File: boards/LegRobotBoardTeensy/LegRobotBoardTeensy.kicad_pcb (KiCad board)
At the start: 2 copper layers, 87.5 x 55 mm, 50 parts, among them J1 B5B-XH-A, J10 B4B-XH-A, J11 B3B-XH-A, J2 B4B-XH-A, J3 B3B-XH-A, J4 B3B-XH-A, J5 B4B-XH-A, J6 B2B-XH-A, J7 B2B-XH-A, J8 B4B-XH-A, J9 B4B-XH-A, Q1 SMMBT3904LT1G, U1 Teensy4.0, U2 TLC555CDR, U3 SN74HC08DR, U4 SN74HC08DR

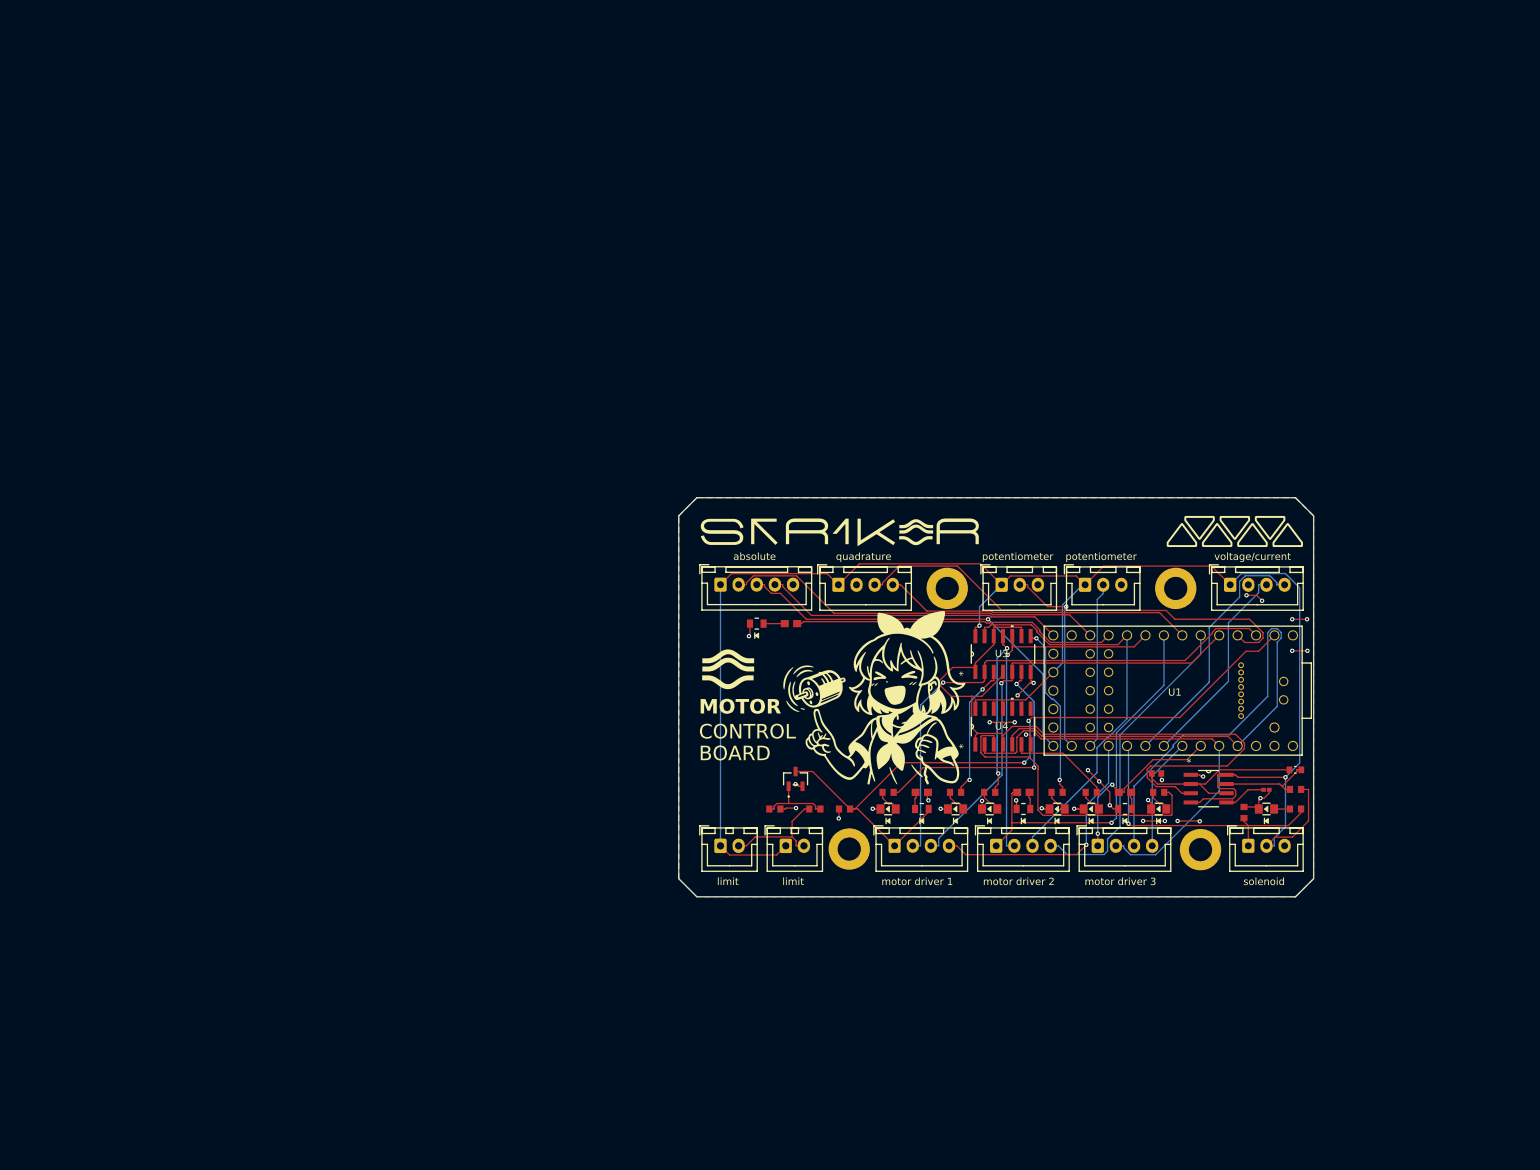
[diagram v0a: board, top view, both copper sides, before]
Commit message: Finalize and order leg board
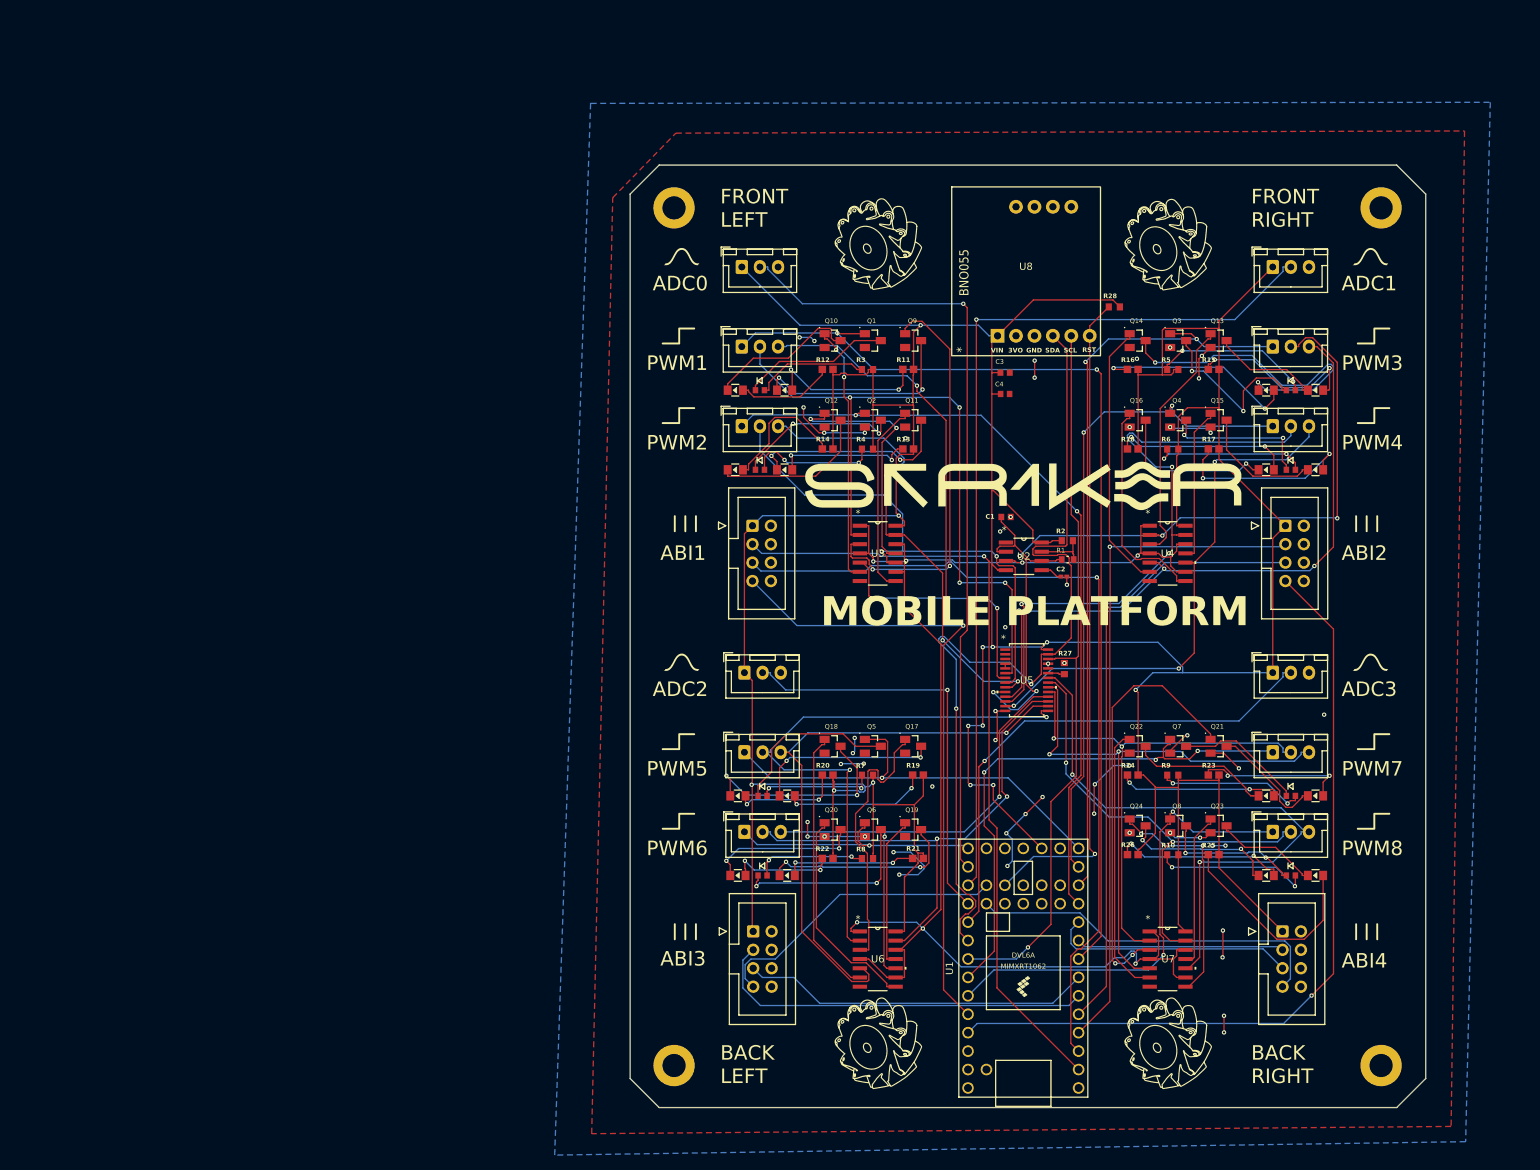
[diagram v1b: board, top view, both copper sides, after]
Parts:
- added C3: 1uF, CC0603JRX7R7BB105:CC0603JRX7R7BB105, F.Cu at (145.0, 56.8)
- added C4: 100nF, CC0603KRX7R9BB104:CC0603KRX7R9BB104, F.Cu at (145.0, 59.7)
- added D12: BLUELED, 150080BS75000:150080BS75000_Modified, F.Cu at (107.8, 70.2)
- added D13: BLUELED, 150080BS75000:150080BS75000_Modified, F.Cu at (187.8, 59.2)
- added D14: BLUELED, 150080BS75000:150080BS75000_Modified, F.Cu at (181.0, 59.2)
- added D15: BLUELED, 150080BS75000:150080BS75000_Modified, F.Cu at (187.8, 70.2)
- added D16: BLUELED, 150080BS75000:150080BS75000_Modified, F.Cu at (181.0, 70.2)
- added D17: BLUELED, 150080BS75000:150080BS75000_Modified, F.Cu at (114.9, 115.1)
- added D18: BLUELED, 150080BS75000:150080BS75000_Modified, F.Cu at (108.2, 115.1)
- added D19: BLUELED, 150080BS75000:150080BS75000_Modified, F.Cu at (114.9, 126.1)
- added D20: BLUELED, 150080BS75000:150080BS75000_Modified, F.Cu at (108.2, 126.1)
- added D21: BLUELED, 150080BS75000:150080BS75000_Modified, F.Cu at (187.8, 115.1)
- added D22: BLUELED, 150080BS75000:150080BS75000_Modified, F.Cu at (181.0, 115.1)
- added D23: BLUELED, 150080BS75000:150080BS75000_Modified, F.Cu at (187.8, 126.1)
- added D24: BLUELED, 150080BS75000:150080BS75000_Modified, F.Cu at (181.0, 126.1)
- added J12: B3B-XH-A, Connector_JST:JST_XH_B3B-XH-A_1x03_P2.50mm_Vertical, F.Cu at (181.9, 109.1)
- added J13: B3B-XH-A, Connector_JST:JST_XH_B3B-XH-A_1x03_P2.50mm_Vertical, F.Cu at (181.9, 120.0)
- added J14: IDC, Connector_IDC:IDC-Header_2x04_P2.54mm_Vertical, F.Cu at (183.6, 77.9)
- added J15: IDC, Connector_IDC:IDC-Header_2x04_P2.54mm_Vertical, F.Cu at (110.3, 133.8)
- added J16: IDC, Connector_IDC:IDC-Header_2x04_P2.54mm_Vertical, F.Cu at (183.2, 133.8)
- added Q10: MMBT3904LT1G, SMMBT3904LT1G:MMBT3904LT1G, F.Cu at (121.2, 52.3)
- added Q11: MMBT3904LT1G, SMMBT3904LT1G:MMBT3904LT1G, F.Cu at (132.3, 63.3)
- added Q12: MMBT3904LT1G, SMMBT3904LT1G:MMBT3904LT1G, F.Cu at (121.2, 63.3)
- added Q13: MMBT3904LT1G, SMMBT3904LT1G:MMBT3904LT1G, F.Cu at (174.4, 52.3)
- added Q14: MMBT3904LT1G, SMMBT3904LT1G:MMBT3904LT1G, F.Cu at (163.2, 52.3)
- added Q15: MMBT3904LT1G, SMMBT3904LT1G:MMBT3904LT1G, F.Cu at (174.4, 63.3)
- added Q16: MMBT3904LT1G, SMMBT3904LT1G:MMBT3904LT1G, F.Cu at (163.2, 63.3)
- added Q17: MMBT3904LT1G, SMMBT3904LT1G:MMBT3904LT1G, F.Cu at (132.3, 108.3)
- added Q18: MMBT3904LT1G, SMMBT3904LT1G:MMBT3904LT1G, F.Cu at (121.2, 108.3)
- added Q19: MMBT3904LT1G, SMMBT3904LT1G:MMBT3904LT1G, F.Cu at (132.3, 119.7)
- added Q2: MMBT3904LT1G, SMMBT3904LT1G:MMBT3904LT1G, F.Cu at (126.8, 63.3)
- added Q20: MMBT3904LT1G, SMMBT3904LT1G:MMBT3904LT1G, F.Cu at (121.2, 119.7)
- added Q21: MMBT3904LT1G, SMMBT3904LT1G:MMBT3904LT1G, F.Cu at (174.4, 108.3)
- added Q22: MMBT3904LT1G, SMMBT3904LT1G:MMBT3904LT1G, F.Cu at (163.2, 108.3)
- added Q23: MMBT3904LT1G, SMMBT3904LT1G:MMBT3904LT1G, F.Cu at (174.4, 119.2)
- added Q24: MMBT3904LT1G, SMMBT3904LT1G:MMBT3904LT1G, F.Cu at (163.2, 119.2)
- added Q3: MMBT3904LT1G, SMMBT3904LT1G:MMBT3904LT1G, F.Cu at (168.8, 52.3)
- added Q4: MMBT3904LT1G, SMMBT3904LT1G:MMBT3904LT1G, F.Cu at (168.8, 63.3)
- added Q5: MMBT3904LT1G, SMMBT3904LT1G:MMBT3904LT1G, F.Cu at (126.8, 108.3)
- added Q6: MMBT3904LT1G, SMMBT3904LT1G:MMBT3904LT1G, F.Cu at (126.8, 119.7)
- added Q7: MMBT3904LT1G, SMMBT3904LT1G:MMBT3904LT1G, F.Cu at (168.8, 108.3)
- added Q8: MMBT3904LT1G, SMMBT3904LT1G:MMBT3904LT1G, F.Cu at (168.8, 119.2)
- added Q9: MMBT3904LT1G, SMMBT3904LT1G:MMBT3904LT1G, F.Cu at (132.3, 52.3)
- added R18: 150R, RC0603FR-07150RL:RESC1607X60N, F.Cu at (162.6, 67.3)
- added R19: 150R, RC0603FR-07150RL:RESC1607X60N, F.Cu at (133.0, 112.2)
- added R20: 150R, RC0603FR-07150RL:RESC1607X60N, F.Cu at (120.5, 112.2)
- added R21: 150R, RC0603FR-07150RL:RESC1607X60N, F.Cu at (133.0, 123.7)
- added R22: 150R, RC0603FR-07150RL:RESC1607X60N, F.Cu at (120.5, 123.7)
- added R23: 150R, RC0603FR-07150RL:RESC1607X60N, F.Cu at (173.7, 112.2)
- added R24: 150R, RC0603FR-07150RL:RESC1607X60N, F.Cu at (162.6, 112.2)
- added R25: 150R, RC0603FR-07150RL:RESC1607X60N, F.Cu at (173.7, 123.2)
- added R26: 150R, RC0603FR-07150RL:RESC1607X60N, F.Cu at (162.6, 123.2)
- added R27: 10K, CRCW060310K0FKEA:CRCW060310K0FKEA, F.Cu at (153.2, 97.5)
- added R28: 10K, CRCW060310K0FKEA:CRCW060310K0FKEA, F.Cu at (160.0, 47.7)
- added U5: PCA9685PW_118, PCA9685PW,118:PCA9685PW,118, F.Cu at (148.0, 99.2)
- added U6: SN74HC08DR, SN74HC08DR:SN74HC08DR, F.Cu at (127.4, 137.6)
- added U7: SN74HC08DR, SN74HC08DR:SN74HC08DR, F.Cu at (167.4, 137.6)
- added U8: BNO055, BNO055:BNO055, F.Cu at (147.9, 42.6)
- D1, D2, D3, D4, D6, D7: value BLUE LED -> REDLED; footprint 150080BS75000:150080BS75000_Modified -> NCD0603R1:NCD0603R1
- D10, D11: value PINK LED -> BLUELED; footprint XL-2012UPC:LED_XL-2012SURC_XLG -> 150080BS75000:150080BS75000_Modified
- D5, D8: value PINK LED -> REDLED; footprint XL-2012UPC:LED_XL-2012SURC_XLG -> NCD0603R1:NCD0603R1
- D9: value BLUE LED -> BLUELED
- J1: value B5B-XH-A -> IDC; footprint Connector_JST:JST_XH_B5B-XH-A_1x05_P2.50mm_Vertical -> Connector_IDC:IDC-Header_2x04_P2.54mm_Vertical
- J10, J2, J5, J8, J9: value B4B-XH-A -> B3B-XH-A; footprint Connector_JST:JST_XH_B4B-XH-A_1x04_P2.50mm_Vertical -> Connector_JST:JST_XH_B3B-XH-A_1x03_P2.50mm_Vertical
- J6, J7: value B2B-XH-A -> B3B-XH-A; footprint Connector_JST:JST_XH_B2B-XH-A_1x02_P2.50mm_Vertical -> Connector_JST:JST_XH_B3B-XH-A_1x03_P2.50mm_Vertical
- Q1: value SMMBT3904LT1G -> MMBT3904LT1G; footprint SMMBT3904LT1G:SMMBT3904LT1G -> SMMBT3904LT1G:MMBT3904LT1G
- R1: value 150R -> 360K; footprint RCG06031K00FKEA:RCG06031K00FKEA -> RC0603FR-07360KL:RC0603FR-07360KL
- R10, R5: value 470R -> 1K; footprint RC0603FR-07470RL:RC0603FR-07470RL -> RCG06031K00FKEA:RCG06031K00FKEA
- R11: footprint RCG06031K00FKEA:RCG06031K00FKEA -> RC0603FR-07150RL:RESC1607X60N
- R12, R13: value 470R -> 150R; footprint RC0603FR-07470RL:RC0603FR-07470RL -> RC0603FR-07150RL:RESC1607X60N
- R14, R17: value 100K -> 150R; footprint CRCW0603100KFKEA:CRCW0603100KFKEA -> RC0603FR-07150RL:RESC1607X60N
- R15: value 10K -> 150R; footprint CRCW060310K0FKEA:CRCW060310K0FKEA -> RC0603FR-07150RL:RESC1607X60N
- R16: value 360K -> 150R; footprint RC0603FR-07360KL:RC0603FR-07360KL -> RC0603FR-07150RL:RESC1607X60N
- R2: value 150R -> 10K; footprint RCG06031K00FKEA:RCG06031K00FKEA -> CRCW060310K0FKEA:CRCW060310K0FKEA
- R3, R4, R6, R7: value 150R -> 1K
- R8: value 10K -> 1K; footprint CRCW060310K0FKEA:CRCW060310K0FKEA -> RCG06031K00FKEA:RCG06031K00FKEA
- R9: value 100K -> 1K; footprint CRCW0603100KFKEA:CRCW0603100KFKEA -> RCG06031K00FKEA:RCG06031K00FKEA
- U1: footprint Teensy:Teensy40_SMT -> Teensy40:Teensy40
- moved D9 88.0 mm to (114.6, 59.2)
- moved J8 86.3 mm to (181.9, 53.2)
- moved D8 81.4 mm to (184.4, 126.1), turned to 180 degrees
- moved R11 80.8 mm to (131.6, 56.3)
- moved D10 70.1 mm to (107.8, 59.2)
- moved J11 69.5 mm to (109.0, 120.0)
- moved J9 69.3 mm to (181.9, 64.1)
- moved J6 68.9 mm to (108.7, 53.2)
- moved R5 67.8 mm to (168.1, 56.3)
- moved D11 66.2 mm to (114.6, 70.2)
- moved D3 66.1 mm to (184.4, 59.2), turned to 180 degrees
- moved MH1 64.6 mm to (99.3, 34.0)
- moved R12 64.2 mm to (120.5, 56.3), turned to 0 degrees
- moved R3 63.9 mm to (126.0, 56.3)
- moved D1 63.7 mm to (111.2, 59.2), turned to 180 degrees
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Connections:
- D1 pad 1: GND -> Net-(D1-K)
- D1 pad 2: Net-(D1-Pad2) -> Net-(D1-A)
- D10 pad 1: GND -> Net-(D10-K)
- D11 pad 1: GND -> Net-(D11-K)
- D2 pad 1: GND -> Net-(D2-K)
- D2 pad 2: Net-(D2-Pad2) -> Net-(D2-A)
- D3 pad 1: GND -> Net-(D3-K)
- D3 pad 2: Net-(D3-Pad2) -> Net-(D3-A)
- D4 pad 1: GND -> Net-(D4-K)
- D4 pad 2: Net-(D4-Pad2) -> Net-(D4-A)
- D5 pad 1: Net-(D5-Pad1) -> Net-(D5-K)
- D5 pad 2: PWM1EN -> Net-(D5-A)
- D6 pad 1: GND -> Net-(D6-K)
- D6 pad 2: Net-(D6-Pad2) -> Net-(D6-A)
- D7 pad 1: GND -> Net-(D7-K)
- D7 pad 2: Net-(D7-Pad2) -> Net-(D7-A)
- D8 pad 1: GND -> Net-(D8-K)
- D9 pad 1: GND -> Net-(D9-K)
- J1 pad 2: CS -> GND
- J1 pad 3: SCK -> ENCODER1_A
- J1 pad 4: MISO -> GND
- J1 pad 5: GND -> ENCODER1_B
- J10 pad 1: PWM3EN -> PWMEN5
- J10 pad 2: RPWM3 -> RPWM5
- J10 pad 3: LPWM3 -> LPWM5
- J11 pad 1: SIG -> PWMEN6
- J11 pad 2: +3.3V -> RPWM6
- J11 pad 3: GND -> LPWM6
- J2 pad 2: GND -> A0
- J2 pad 3: A -> GND
- J3 pad 2: A0 -> A1
- J4 pad 2: A1 -> A2
- J5 pad 2: GND -> A3
- J5 pad 3: SCL -> GND
- J6 pad 1: +3.3V -> PWMEN1
- J6 pad 2: /PWM1EN_LIMIT_KILL -> RPWM1
- J7 pad 1: +3.3V -> PWMEN2
- J7 pad 2: /PWM1EN_LIMIT_KILL -> RPWM2
- J8 pad 1: PWM1EN -> PWMEN3
- J8 pad 2: RPWM1 -> RPWM3
- J8 pad 3: LPWM1 -> LPWM3
- J9 pad 1: PWM2EN -> PWMEN4
- J9 pad 2: RPWM2 -> RPWM4
- J9 pad 3: LPWM2 -> LPWM4
- Q1 pad 1: Net-(Q1-BASE) -> PWMEN1
- Q1 pad 3: PWM1EN -> Net-(D1-K)
- R1 pad 1: Net-(D1-Pad2) -> /NODE_A
- R1 pad 2: RPWM1A -> /NODE_B
- R10 pad 2: SPIS -> +3.3V
- R11 pad 2: SIG -> +3.3V
- R12 pad 2: PWM2EN -> +3.3V
- R13 pad 2: PWM3EN -> +3.3V
- R14 pad 1: GND -> Net-(D12-A)
- R14 pad 2: Net-(Q1-BASE) -> +3.3V
- R15 pad 1: /NODE_B -> Net-(D13-A)
- R16 pad 1: /NODE_A -> Net-(D14-A)
- R16 pad 2: /NODE_B -> +3.3V
- R17 pad 1: GND -> Net-(D15-A)
- R17 pad 2: SIG -> +3.3V
- R2 pad 1: Net-(D2-Pad2) -> +3.3V
- R2 pad 2: LPWM1A -> /NODE_B
- R3 pad 1: Net-(D3-Pad2) -> Net-(D1-A)
- R3 pad 2: RPWM2A -> +3.3V
- R4 pad 1: Net-(D4-Pad2) -> Net-(D2-A)
- R4 pad 2: LPWM2A -> +3.3V
- R5 pad 1: Net-(D5-Pad1) -> Net-(D3-A)
- R5 pad 2: GND -> +3.3V
- R6 pad 1: Net-(D6-Pad2) -> Net-(D4-A)
- R6 pad 2: RPWM3A -> +3.3V
- R7 pad 1: Net-(D7-Pad2) -> Net-(D5-A)
- R7 pad 2: LPWM3A -> +3.3V
- R8 pad 1: /PWM1EN_LIMIT_KILL -> Net-(D6-A)
- R8 pad 2: Net-(Q1-BASE) -> +3.3V
- R9 pad 1: GND -> Net-(D7-A)
- R9 pad 2: PWM1EN -> +3.3V
- U1 pad 10: LPWM2 -> ENCODER4_B
- U1 pad 11: SPIS -> PWMEN2
- U1 pad 12: CS -> PWMEN3
- U1 pad 13: unconnected-(U1-11_MOSI_CTX1-Pad13) -> PWMEN4
- U1 pad 14: MISO -> PWMEN5
- U1 pad 17: unconnected-(U1-GND-Pad17) -> GND
- U1 pad 2: PWM1EN -> ENCODER1_A
- U1 pad 20: SCK -> PWMEN6
- U1 pad 23: PWM1VT -> A2
- U1 pad 24: SIG -> A3
- U1 pad 27: PWM3VT -> PWMEN7
- U1 pad 28: PWM3EN -> PWMEN8
- U1 pad 29: RPWM3 -> ENCODER1_I
- U1 pad 3: RPWM1 -> ENCODER1_B
- U1 pad 30: LPWM3 -> ENCODER2_I
- U1 pad 35: unconnected-(U1-24_A10_TX6_SCL2-Pad35) -> ENCODER3_I
- U1 pad 36: unconnected-(U1-25_A11_RX6_SDA2-Pad36) -> ENCODER4_I
- U1 pad 37: unconnected-(U1-26_A12_MOSI1-Pad37) -> RST
- U1 pad 4: A -> ENCODER2_A
- U1 pad 5: LPWM1 -> ENCODER2_B
- U1 pad 6: PWM2VT -> ENCODER3_A
- U1 pad 7: B -> ENCODER3_B
- U1 pad 8: PWM2EN -> PWMEN1
- U1 pad 9: RPWM2 -> ENCODER4_A
- U3 pad 11: LPWM2A -> LPWM2BLINK
- U3 pad 3: RPWM1A -> RPWM1BLINK
- U3 pad 6: LPWM1A -> LPWM1BLINK
- U3 pad 8: RPWM2A -> RPWM2BLINK
- U4 pad 10: unconnected-(U4-3B-Pad10) -> LPWM4
- U4 pad 11: unconnected-(U4-4Y-Pad11) -> RPWM4BLINK
- U4 pad 12: unconnected-(U4-4A-Pad12) -> BLINK
- U4 pad 13: unconnected-(U4-4B-Pad13) -> RPWM4
- U4 pad 3: RPWM3A -> RPWM3BLINK
- U4 pad 6: LPWM3A -> LPWM3BLINK
- U4 pad 8: unconnected-(U4-3Y-Pad8) -> LPWM4BLINK
- U4 pad 9: unconnected-(U4-3A-Pad9) -> BLINK
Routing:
- net +3.3V: track 242.3 -> 627.7 mm, vias 2 -> 13
- net PWMEN1: track 0.00 -> 138.4 mm, vias 0 -> 2
- net ENCODER1_B: track 0.00 -> 117.0 mm, vias 0 -> 1
- net ENCODER2_I: track 0.00 -> 110.6 mm, vias 0 -> 1
- net PWMEN2: track 0.00 -> 109.3 mm, vias 0 -> 2
- net ENCODER1_A: track 0.00 -> 108.8 mm, vias 0 -> 1
- net PWMEN3: track 0.00 -> 104.2 mm, vias 0 -> 2
- net BLINK: track 99.7 -> 203.2 mm, vias 0 -> 7
- net A1: track 23.0 -> 125.1 mm, vias 0 -> 1
- net PWM1EN: track 96.5 -> 0.00 mm, vias 2 -> 0
- net ENCODER2_A: track 0.00 -> 93.1 mm, vias 0 -> 1
- net PWMEN4: track 0.00 -> 91.1 mm, vias 0 -> 2
- net RST: track 0.00 -> 91.0 mm, vias 0 -> 1
- net ENCODER1_I: track 0.00 -> 87.7 mm, vias 0 -> 1
- net SDA: track 35.3 -> 122.6 mm, vias 0 -> 2
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- added copper zone on F.Cu, net GND
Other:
- board size 87.5 x 55 mm -> 109.6 x 129.9 mm
- board text added: "ABI1"
- board text added: "ABI2"
- board text added: "ABI3"
- board text added: "ABI4"
- board text added: "ADC0"
- board text added: "ADC1"
- board text added: "ADC2"
- board text added: "ADC3"
- board text added: "BACK LEFT"
- board text added: "BACK RIGHT"
- board text added: "FRONT LEFT"
- board text added: "FRONT RIGHT"
- board text added: "MOBILE PLATFORM"
- board text added: "PWM1"
- board text added: "PWM2"
- board text added: "PWM3"
- board text added: "PWM4"
- board text added: "PWM5"
- board text added: "PWM6"
- board text added: "PWM7"
- board text added: "PWM8"
- board text removed: "BOARD"
- board text removed: "CONTROL"
- board text removed: "MOTOR"
- board text removed: "absolute"
- board text removed: "limit"
- board text removed: "motor driver 1"
- board text removed: "motor driver 2"
- board text removed: "motor driver 3"
- board text removed: "potentiometer"
- board text removed: "quadrature"
- board text removed: "solenoid"
- board text removed: "voltage/current"

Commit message: Update main and leg board
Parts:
- added C5: 47nF, CL10B473KB8NNNC:CAPC1608X90N, F.Cu at (37.0, 46.8)
- added C6: 47nF, CL10B473KB8NNNC:CAPC1608X90N, F.Cu at (37.0, 49.2)
- added C7: 47nF, CL10B473KB8NNNC:CAPC1608X90N, F.Cu at (37.0, 51.7)
- added C8: 47nF, CL10B473KB8NNNC:CAPC1608X90N, F.Cu at (37.0, 54.2)
- added R29: 2.2K, RC0603FR-072K2L:RC0603FR-072K2L, F.Cu at (33.0, 46.8)
- added R30: 2.2K, RC0603FR-072K2L:RC0603FR-072K2L, F.Cu at (33.0, 49.4)
- added R31: 2.2K, RC0603FR-072K2L:RC0603FR-072K2L, F.Cu at (33.0, 52.0)
- added R32: 2.2K, RC0603FR-072K2L:RC0603FR-072K2L, F.Cu at (33.0, 54.5)
- J10, J11, J12, J13, J6, J7, J8, J9: value B3B-XH-A -> IDC; footprint Connector_JST:JST_XH_B3B-XH-A_1x03_P2.50mm_Vertical -> Connector_IDC:IDC-Header_2x04_P2.54mm_Vertical
- moved U6 21.8 mm to (130.9, 116.1)
- moved U7 21.8 mm to (164.1, 116.0)
- moved R8 17.9 mm to (132.1, 106.9)
- moved R21 17.9 mm to (139.1, 106.9)
- moved R22 17.9 mm to (126.6, 106.9)
- moved Q19 17.9 mm to (138.4, 103.0)
- moved Q20 17.9 mm to (127.3, 103.0)
- moved Q6 17.9 mm to (132.8, 103.0)
- moved Q23 17.0 mm to (170.1, 102.8)
- moved Q24 17.0 mm to (158.9, 102.8)
- moved Q8 17.0 mm to (164.5, 102.8)
- moved R25 17.0 mm to (169.4, 106.8)
- moved R26 17.0 mm to (158.2, 106.8)
- moved R10 17.0 mm to (163.8, 106.8)
- moved Q17 16.4 mm to (138.4, 93.0)
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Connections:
- J10 pad 1: PWMEN5 -> GND
- J10 pad 2: RPWM5 -> +3.3V
- J10 pad 3: LPWM5 -> L_IS5
- J11 pad 1: PWMEN6 -> GND
- J11 pad 2: RPWM6 -> +3.3V
- J11 pad 3: LPWM6 -> L_IS6
- J12 pad 1: PWMEN7 -> GND
- J12 pad 2: RPWM7 -> +3.3V
- J12 pad 3: LPWM7 -> L_IS7
- J13 pad 1: PWMEN8 -> GND
- J13 pad 2: RPWM8 -> +3.3V
- J13 pad 3: LPWM8 -> L_IS8
- J2 pad 2: A0 -> Net-(J2-Pin_2)
- J3 pad 2: A1 -> Net-(J3-Pin_2)
- J4 pad 2: A2 -> Net-(J4-Pin_2)
- J5 pad 2: A3 -> Net-(J5-Pin_2)
- J6 pad 1: PWMEN1 -> GND
- J6 pad 2: RPWM1 -> +3.3V
- J6 pad 3: LPWM1 -> L_IS1
- J7 pad 1: PWMEN2 -> GND
- J7 pad 2: RPWM2 -> +3.3V
- J7 pad 3: LPWM2 -> L_IS2
- J8 pad 1: PWMEN3 -> GND
- J8 pad 2: RPWM3 -> +3.3V
- J8 pad 3: LPWM3 -> L_IS3
- J9 pad 1: PWMEN4 -> GND
- J9 pad 2: RPWM4 -> +3.3V
- J9 pad 3: LPWM4 -> L_IS4
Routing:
- net +3.3V: track 627.7 -> 0.00 mm, vias 13 -> 0
- net BLINK: track 203.2 -> 0.00 mm, vias 7 -> 0
- net PWMEN1: track 138.4 -> 0.00 mm, vias 2 -> 0
- net A1: track 125.1 -> 0.00 mm, vias 1 -> 0
- net SDA: track 122.6 -> 0.00 mm, vias 2 -> 0
- net ENCODER1_B: track 117.0 -> 0.00 mm, vias 1 -> 0
- net ENCODER2_I: track 110.6 -> 0.00 mm, vias 1 -> 0
- net PWMEN2: track 109.3 -> 0.00 mm, vias 2 -> 0
- net A0: track 108.9 -> 0.00 mm, vias 1 -> 0
- net ENCODER1_A: track 108.8 -> 0.00 mm, vias 1 -> 0
- net RPWM3: track 107.4 -> 0.00 mm, vias 5 -> 0
- net PWMEN3: track 104.2 -> 0.00 mm, vias 2 -> 0
- net GND: track 103.1 -> 0.00 mm, vias 53 -> 0
- net SCL: track 100.4 -> 0.00 mm, vias 1 -> 0
- net RPWM1: track 96.9 -> 0.00 mm, vias 4 -> 0
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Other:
- board size 109.6 x 129.9 mm -> 109.6 x 116.6 mm
- board text removed: "BACK LEFT"
- board text removed: "BACK RIGHT"
- board text removed: "FRONT LEFT"
- board text removed: "FRONT RIGHT"
- board text removed: "MOBILE PLATFORM"
